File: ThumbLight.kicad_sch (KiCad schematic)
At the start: 1 part

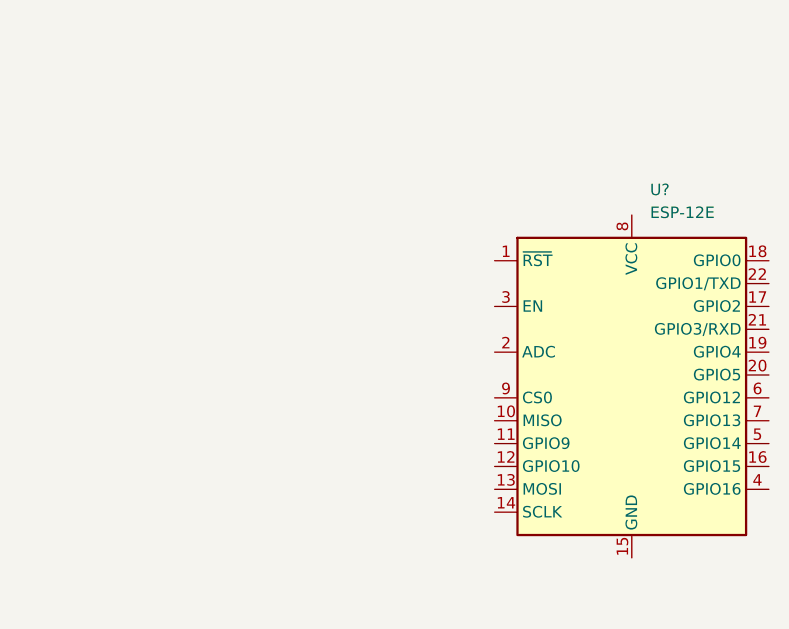
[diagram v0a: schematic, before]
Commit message: Add TP4056 module
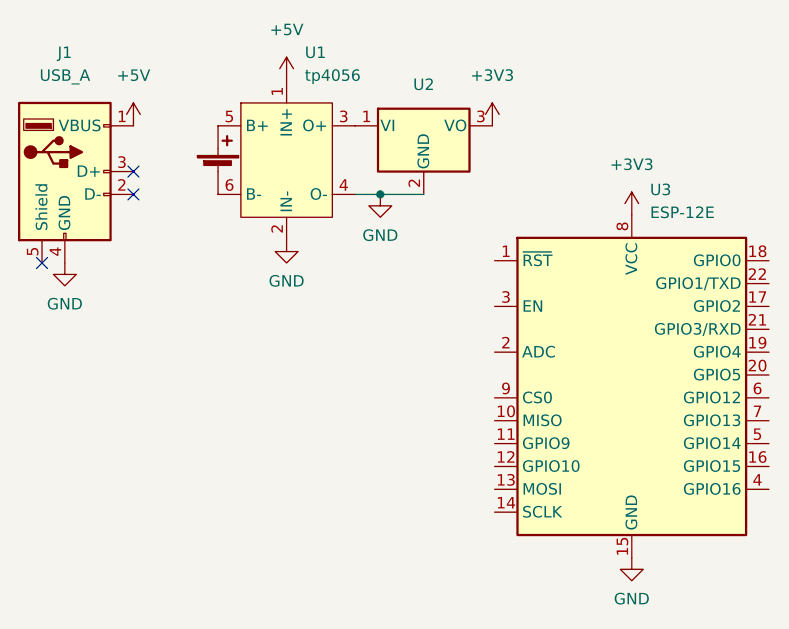
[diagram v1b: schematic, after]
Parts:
- added BT1: Battery_Cell, symbol Device:Battery_Cell
- added J1: USB_A, symbol Connector:USB_A
- added U1: tp4056, tp4056:tp4056, symbol TP4056:TP4056
- added U2: UA78M33_TO252, Package_TO_SOT_SMD:TO-252-2, symbol Regulator_Linear:KA78M05_TO252
- gave numbers to parts that had none: 1
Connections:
- net GND: now reaches U3.15 (GND)
- net GND: now also J1.4 (GND), U1.2 (IN-), U1.4 (O-), U2.2 (GND)
- net +3V3: now reaches U3.8 (VCC)
- net +3V3: now also U2.3 (VO)
- new net: U1.3 (O+), U2.1 (VI)
- new net: BT1.1 (+), U1.5 (B+)
- new net: BT1.2 (-), U1.6 (B-)
- new net +5V: J1.1 (VBUS), U1.1 (IN+)
- no-connect marks 0 -> 3
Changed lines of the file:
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@@
 (kicad_sch (version 20211123) (generator eeschema)
   (paper "A4")
+  (junction (at 98.044 41.148) (diameter 0) (color 0 0 0 0)
+  )
+  (no_connect (at 70.612 38.608))
+  (no_connect (at 60.452 48.768))
+  (no_connect (at 70.612 41.148))
+  (wire (pts (xy 95.25 41.148) (xy 98.044 41.148))
+    (stroke (width 0) (type default) (color 0 0 0 0))
+  )
+  (wire (pts (xy 98.044 41.148) (xy 102.87 41.148))
+    (stroke (width 0) (type default) (color 0 0 0 0))
+  )
+  (symbol (lib_id "TP4056:TP4056") (at 87.63 37.338 0) (unit 1)
+    (in_bom yes) (on_board yes) (fields_autoplaced)
+    (property "Reference" "U1" (id 0) (at 89.6494 25.4 0)
+      (effects (font (size 1.27 1.27)) (justify left))
+    )
+    (property "Value" "tp4056" (id 1) (at 89.6494 27.94 0)
+      (effects (font (size 1.27 1.27)) (justify left))
+    )
+    (property "Footprint" "tp4056:tp4056" (id 2) (at 86.36 11.303 0)
+      (effects (font (size 1.27 1.27)) hide)
+    )
+    (property "Datasheet" "" (id 3) (at 86.36 11.303 0)
+      (effects (font (size 1.27 1.27)) hide)
+    )
+    (pin "1")
+    (pin "2")
+    (pin "3")
+    (pin "4")
+    (pin "5")
+    (pin "6")
+  )
+  (symbol (lib_id "Device:Battery_Cell") (at 80.01 38.608 0) (unit 1)
+    (in_bom yes) (on_board yes)
+    (property "Reference" "BT1" (id 0) (at 75.692 35.306 0)
+      (effects (font (size 1.27 1.27)) (justify left) hide)
+    )
+    (property "Value" "Battery_Cell" (id 1) (at 84.074 37.8459 0)
+      (effects (font (size 1.27 1.27)) (justify left) hide)
+    )
+    (property "Footprint" "" (id 2) (at 80.01 37.084 90)
+      (effects (font (size 1.27 1.27)) hide)
+    )
+    (property "Datasheet" "~" (id 3) (at 80.01 37.084 90)
+      (effects (font (size 1.27 1.27)) hide)
+    )
+    (pin "1")
+    (pin "2")
+  )
+  (symbol (lib_id "power:+5V") (at 87.63 28.448 0) (unit 1)
+    (in_bom yes) (on_board yes) (fields_autoplaced)
+    (property "Reference" "#PWR0103" (id 0) (at 87.63 32.258 0)
+      (effects (font (size 1.27 1.27)) hide)
+    )
+    (property "Value" "+5V" (id 1) (at 87.63 22.86 0))
+    (property "Footprint" "" (id 2) (at 87.63 28.448 0)
+      (effects (font (size 1.27 1.27)) hide)
+    )
+    (property "Datasheet" "" (id 3) (at 87.63 28.448 0)
+      (effects (font (size 1.27 1.27)) hide)
+    )
+    (pin "1")
+  )
+  (symbol (lib_id "power:GND") (at 87.63 46.228 0) (unit 1)
+    (in_bom yes) (on_board yes) (fields_autoplaced)
+    (property "Reference" "#PWR0104" (id 0) (at 87.63 52.578 0)
+      (effects (font (size 1.27 1.27)) hide)
+    )
+    (property "Value" "GND" (id 1) (at 87.63 50.8 0))
+    (property "Footprint" "" (id 2) (at 87.63 46.228 0)
+      (effects (font (size 1.27 1.27)) hide)
+    )
+    (property "Datasheet" "" (id 3) (at 87.63 46.228 0)
+      (effects (font (size 1.27 1.27)) hide)
+    )
+    (pin "1")
+  )
+  (symbol (lib_id "power:GND") (at 125.984 81.534 0) (unit 1)
+    (in_bom yes) (on_board yes) (fields_autoplaced)
+    (property "Reference" "#PWR0108" (id 0) (at 125.984 87.884 0)
+      (effects (font (size 1.27 1.27)) hide)
+    )
+    (property "Value" "GND" (id 1) (at 125.984 86.106 0))
+    (property "Footprint" "" (id 2) (at 125.984 81.534 0)
+      (effects (font (size 1.27 1.27)) hide)
+    )
+    (property "Datasheet" "" (id 3) (at 125.984 81.534 0)
+      (effects (font (size 1.27 1.27)) hide)
+    )
+    (pin "1")
+  )
+  (symbol (lib_id "power:+3V3") (at 110.49 33.528 0) (unit 1)
+    (in_bom yes) (on_board yes) (fields_autoplaced)
+    (property "Reference" "#PWR0106" (id 0) (at 110.49 37.338 0)
+      (effects (font (size 1.27 1.27)) hide)
+    )
+    (property "Value" "+3V3" (id 1) (at 110.49 27.94 0))
+    (property "Footprint" "" (id 2) (at 110.49 33.528 0)
+      (effects (font (size 1.27 1.27)) hide)
+    )
+    (property "Datasheet" "" (id 3) (at 110.49 33.528 0)
+      (effects (font (size 1.27 1.27)) hide)
+    )
+    (pin "1")
+  )
+  (symbol (lib_id "power:+5V") (at 70.612 33.528 0) (unit 1)
+    (in_bom yes) (on_board yes) (fields_autoplaced)
+    (property "Reference" "#PWR0101" (id 0) (at 70.612 37.338 0)
+      (effects (font (size 1.27 1.27)) hide)
+    )
+    (property "Value" "+5V" (id 1) (at 70.612 27.94 0))
+    (property "Footprint" "" (id 2) (at 70.612 33.528 0)
+      (effects (font (size 1.27 1.27)) hide)
+    )
+    (property "Datasheet" "" (id 3) (at 70.612 33.528 0)
+      (effects (font (size 1.27 1.27)) hide)
+    )
+    (pin "1")
+  )
   (symbol (lib_id "RF_Module:ESP-12E") (at 125.984 63.754 0) (unit 1)
     (in_bom yes) (on_board yes) (fields_autoplaced)
-    (property "Reference" "U?" (id 0) (at 128.0034 40.64 0)
+    (property "Reference" "U3" (id 0) (at 128.0034 40.64 0)
       (effects (font (size 1.27 1.27)) (justify left))
     )
@@
     (pin "9")
   )
+  (symbol (lib_id "Connector:USB_A") (at 62.992 38.608 0) (unit 1)
+    (in_bom yes) (on_board yes) (fields_autoplaced)
+    (property "Reference" "J1" (id 0) (at 62.992 25.4 0))
+    (property "Value" "USB_A" (id 1) (at 62.992 27.94 0))
+    (property "Footprint" "" (id 2) (at 66.802 39.878 0)
+      (effects (font (size 1.27 1.27)) hide)
+    )
+    (property "Datasheet" " ~" (id 3) (at 66.802 39.878 0)
+      (effects (font (size 1.27 1.27)) hide)
+    )
+    (pin "1")
+    (pin "2")
+    (pin "3")
+    (pin "4")
+    (pin "5")
+  )
+  (symbol (lib_id "power:GND") (at 62.992 48.768 0) (unit 1)
+    (in_bom yes) (on_board yes) (fields_autoplaced)
+    (property "Reference" "#PWR0102" (id 0) (at 62.992 55.118 0)
+      (effects (font (size 1.27 1.27)) hide)
+    )
+    (property "Value" "GND" (id 1) (at 62.992 53.34 0))
+    (property "Footprint" "" (id 2) (at 62.992 48.768 0)
+      (effects (font (size 1.27 1.27)) hide)
+    )
+    (property "Datasheet" "" (id 3) (at 62.992 48.768 0)
+      (effects (font (size 1.27 1.27)) hide)
+    )
+    (pin "1")
+  )
+  (symbol (lib_id "power:+3V3") (at 125.984 43.434 0) (unit 1)
+    (in_bom yes) (on_board yes) (fields_autoplaced)
+    (property "Reference" "#PWR0107" (id 0) (at 125.984 47.244 0)
+      (effects (font (size 1.27 1.27)) hide)
+    )
+    (property "Value" "+3V3" (id 1) (at 125.984 37.846 0))
+    (property "Footprint" "" (id 2) (at 125.984 43.434 0)
+      (effects (font (size 1.27 1.27)) hide)
+    )
+    (property "Datasheet" "" (id 3) (at 125.984 43.434 0)
+      (effects (font (size 1.27 1.27)) hide)
+    )
+    (pin "1")
+  )
+  (symbol (lib_id "Regulator_Linear:KA78M05_TO252") (at 102.87 33.528 0) (unit 1)
+    (in_bom yes) (on_board yes)
+    (property "Reference" "U2" (id 0) (at 102.87 28.956 0))
+    (property "Value" "UA78M33_TO252" (id 1) (at 102.87 28.956 0)
+      (effects (font (size 1.27 1.27)) hide)
+    )
+    (property "Footprint" "Package_TO_SOT_SMD:TO-252-2" (id 2) (at 102.87 27.813 0)
+      (effects (font (size 1.27 1.27) italic) hide)
+    )
+    (property "Datasheet" "https://www.onsemi.com/pub/Collateral/MC78M00-D.PDF" (id 3) (at 102.87 34.798 0)
+      (effects (font (size 1.27 1.27)) hide)
+    )
+    (pin "1")
+    (pin "2")
+    (pin "3")
+  )
+  (symbol (lib_id "power:GND") (at 98.044 41.148 0) (unit 1)
+    (in_bom yes) (on_board yes) (fields_autoplaced)
+    (property "Reference" "#PWR0105" (id 0) (at 98.044 47.498 0)
+      (effects (font (size 1.27 1.27)) hide)
+    )
+    (property "Value" "GND" (id 1) (at 98.044 45.72 0))
+    (property "Footprint" "" (id 2) (at 98.044 41.148 0)
+      (effects (font (size 1.27 1.27)) hide)
+    )
+    (property "Datasheet" "" (id 3) (at 98.044 41.148 0)
+      (effects (font (size 1.27 1.27)) hide)
+    )
+    (pin "1")
+  )
   (sheet_instances
     (path "/" (page "1"))
   )
   (symbol_instances
+    (path "/77aafe58-15f7-410d-963b-841b7cedc81b"
+      (reference "#PWR0101") (unit 1) (value "+5V") (footprint "")
+    )
+    (path "/b8988862-6f0c-4cea-a3a9-4435540a23f6"
+      (reference "#PWR0102") (unit 1) (value "GND") (footprint "")
+    )
+    (path "/5b2a43c2-f205-4722-aaa9-b9d3a2788bfd"
+      (reference "#PWR0103") (unit 1) (value "+5V") (footprint "")
+    )
+    (path "/5b5d48bc-a02d-4228-b920-49510bdec6ad"
+      (reference "#PWR0104") (unit 1) (value "GND") (footprint "")
+    )
+    (path "/fd836c71-13a9-4b30-b3f7-fb9c09a965c0"
+      (reference "#PWR0105") (unit 1) (value "GND") (footprint "")
+    )
+    (path "/73e46a7e-ab55-48cc-aacd-3ec8c2bad971"
+      (reference "#PWR0106") (unit 1) (value "+3V3") (footprint "")
+    )
+    (path "/c199123d-eb7c-4101-9925-a976cd3224b4"
+      (reference "#PWR0107") (unit 1) (value "+3V3") (footprint "")
+    )
+    (path "/6571597a-37e3-47a8-b24c-14045a5b6621"
+      (reference "#PWR0108") (unit 1) (value "GND") (footprint "")
+    )
+    (path "/4a7017ab-22d3-4a17-bb1c-024ea646a95a"
+      (reference "BT1") (unit 1) (value "Battery_Cell") (footprint "")
+    )
+    (path "/b11863f2-05f0-4c70-9612-53388c5c7348"
+      (reference "J1") (unit 1) (value "USB_A") (footprint "")
+    )
+    (path "/3977443d-a1aa-4799-947e-415d942488ea"
+      (reference "U1") (unit 1) (value "tp4056") (footprint "tp4056:tp4056")
+    )
+    (path "/efad0331-27eb-4636-86a4-200955527a64"
+      (reference "U2") (unit 1) (value "UA78M33_TO252") (footprint "Package_TO_SOT_SMD:TO-252-2")
+    )
     (path "/83da7b4d-029d-4f5f-ab78-15c0cc6216c2"
-      (reference "U?") (unit 1) (value "ESP-12E") (footprint "RF_Module:ESP-12E")
-    )
-  )
+      (reference "U3") (unit 1) (value "ESP-12E") (footprint "RF_Module:ESP-12E")
+    )
+  )

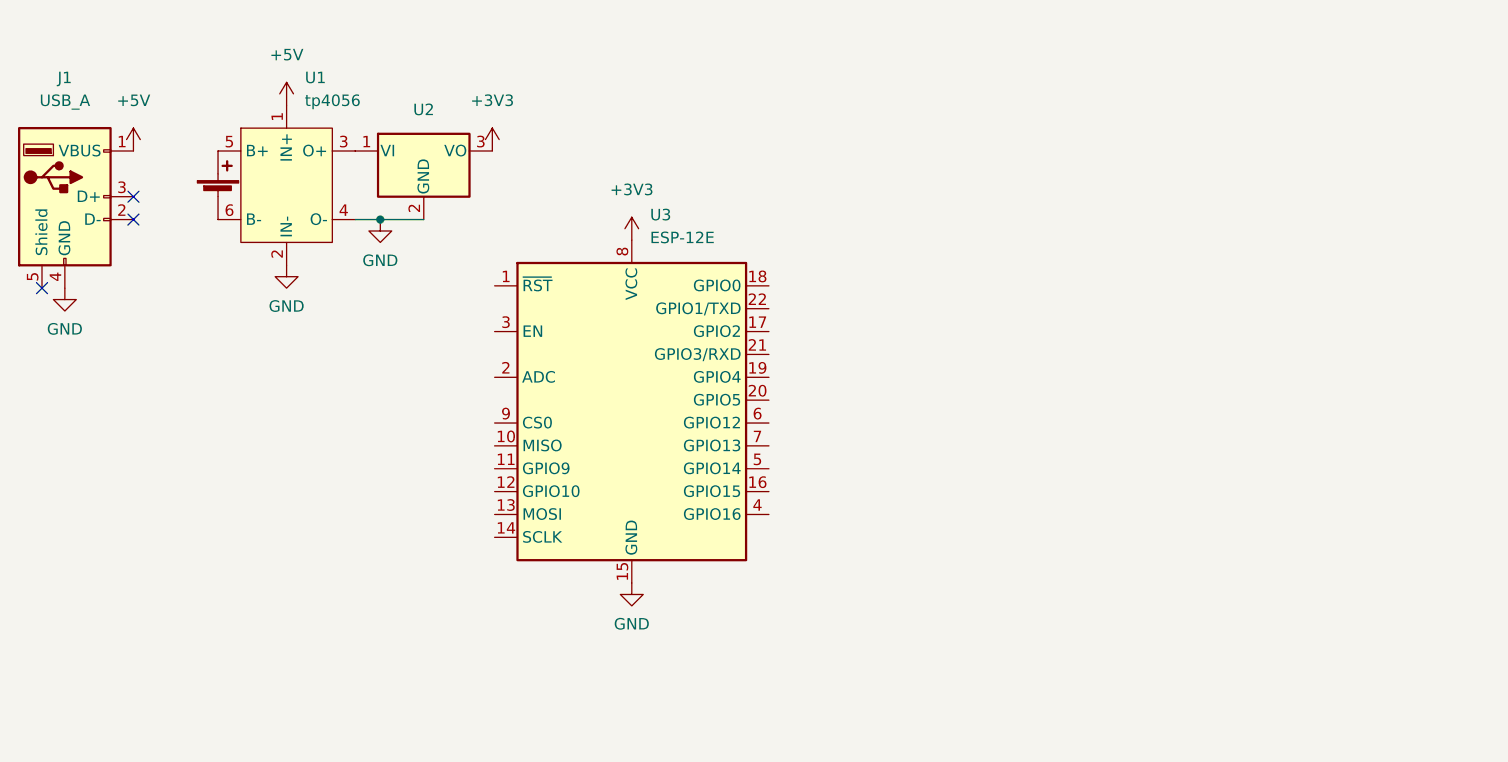
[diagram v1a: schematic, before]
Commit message: rough layout and remove battery functionality
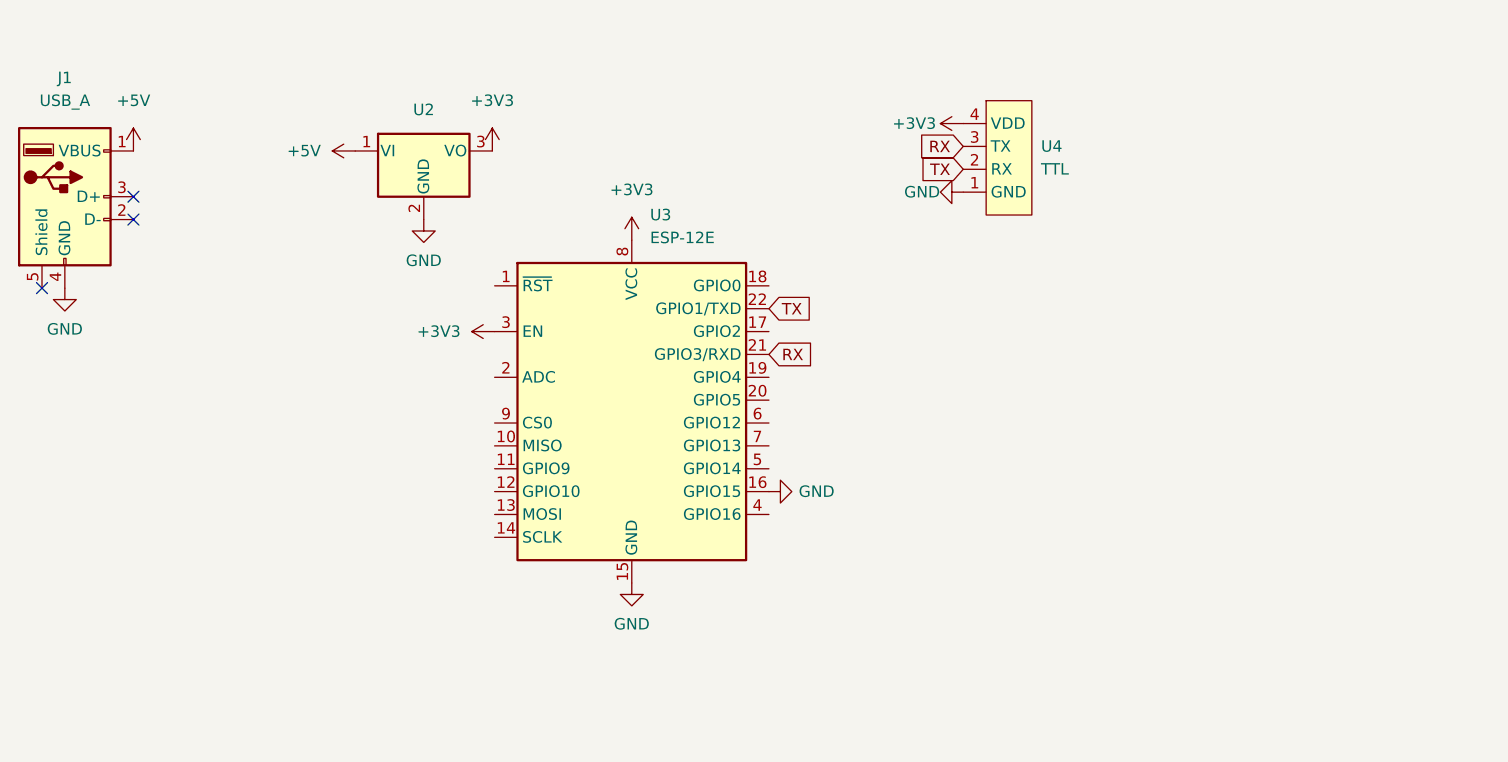
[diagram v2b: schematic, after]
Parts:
- removed BT1: Battery_Cell, symbol Device:Battery_Cell
- removed U1: tp4056, tp4056:tp4056, symbol TP4056:TP4056
- added U4: TTL, Connector_PinHeader_2.54mm:PinHeader_1x04_P2.54mm_Vertical, symbol ftdi-connector:TTL
- J1: footprint (none) -> Connector_USB:USB_A_CNCTech_1001-011-01101_Horizontal
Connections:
- net +3V3: now also U3.3 (EN), U4.4 (VDD)
- net +5V: now also U2.1 (VI)
- net GND: now also U3.16 (GPIO15), U4.1 (GND)
- net RX: now reaches U3.21 (GPIO3/RXD)
- net RX: now also U4.3 (TX)
- net TX: now reaches U3.22 (GPIO1/TXD)
- net TX: now also U4.2 (RX)
